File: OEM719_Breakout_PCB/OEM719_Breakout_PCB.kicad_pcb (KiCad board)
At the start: 2 copper layers, 165 x 61 mm, 27 parts, among them J1 Conn_02x10_Odd_Even, J2 Conn_02x10_Odd_Even, J3 Picoblade, J4 2.54mm Header, J5 2.54mm Socket

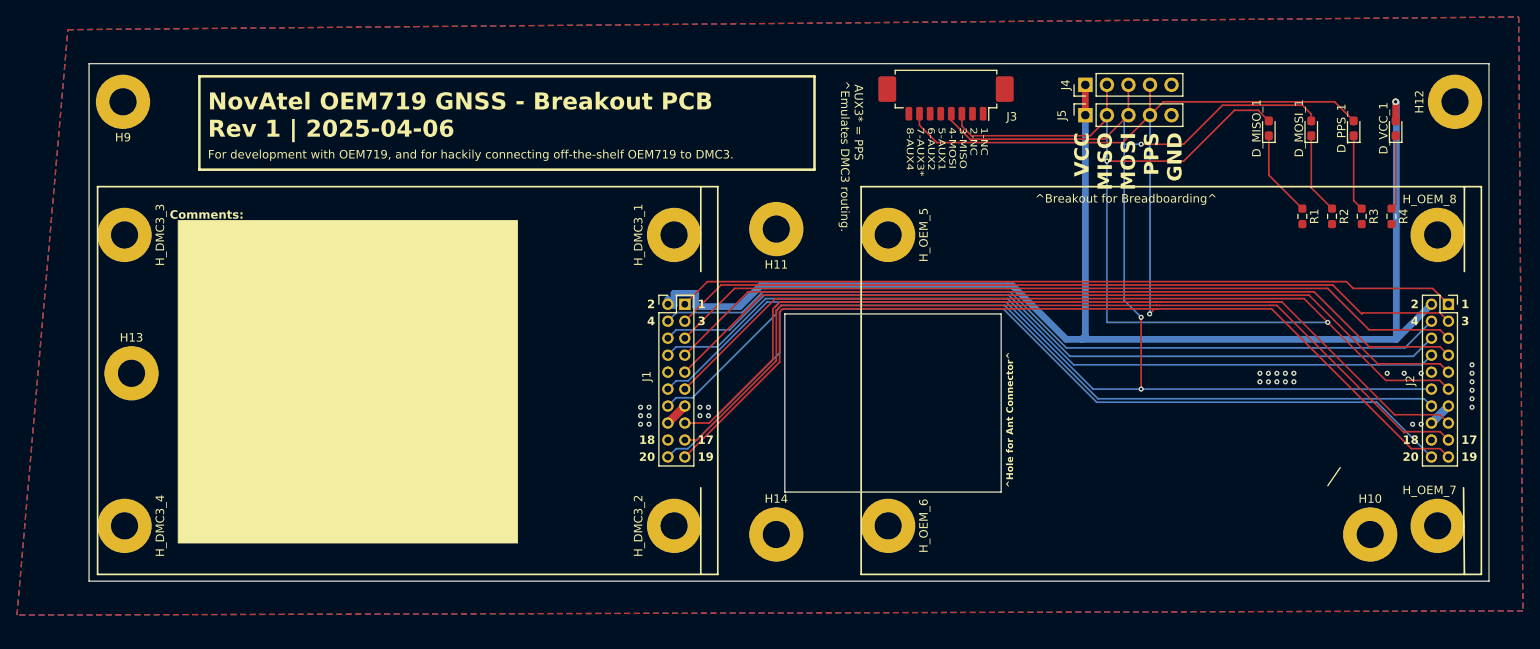
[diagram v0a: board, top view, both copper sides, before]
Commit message: Add 20-pin 2.54mm full breakout
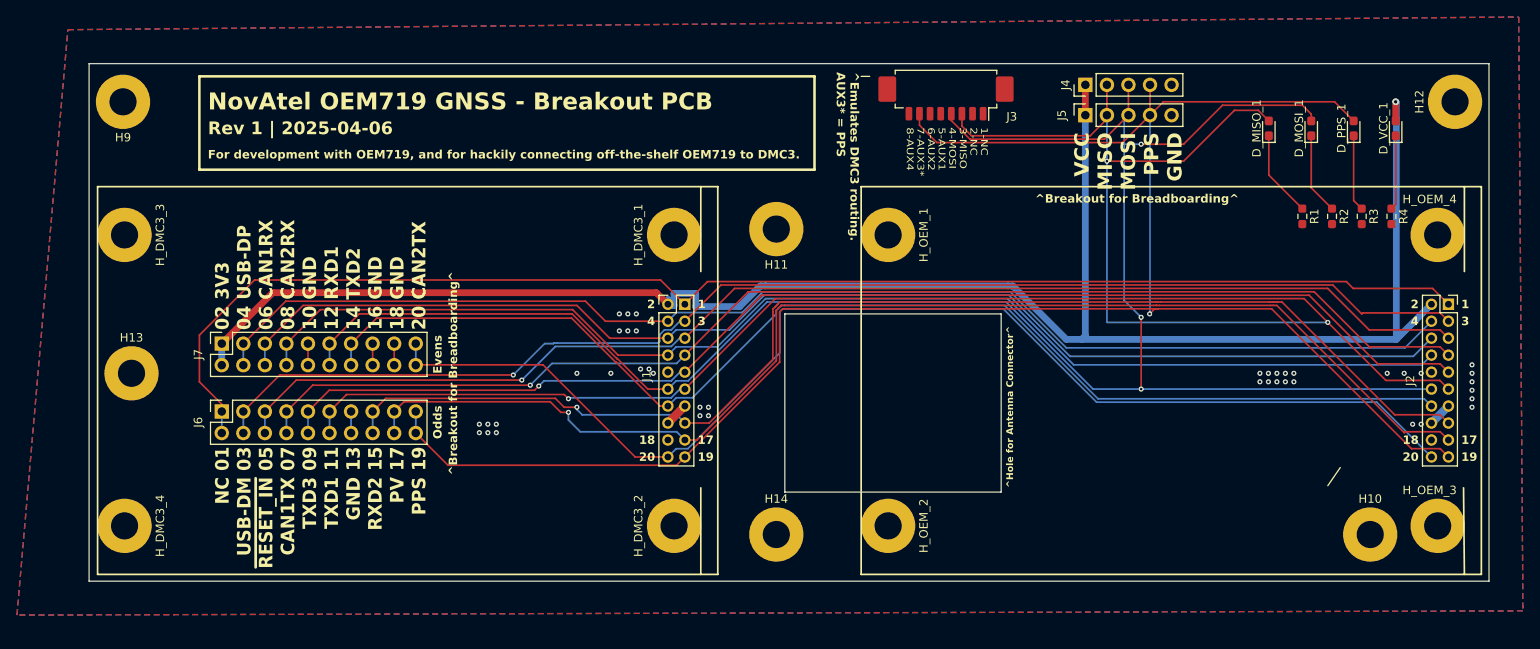
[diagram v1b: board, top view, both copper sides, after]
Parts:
- added J6: Conn_02x10_Odd_Even, 00-footprint-lib:PinHeaderSocket_2x10_P2.54mm_Vertical, F.Cu at (44.6, 111.5)
- added J7: Conn_02x10_Odd_Even, 00-footprint-lib:PinHeaderSocket_2x10_P2.54mm_Vertical, F.Cu at (44.6, 103.5)
- renumbered H_OEM_5 to H_OEM_1, H_OEM_6 to H_OEM_2, H_OEM_7 to H_OEM_3, H_OEM_8 to H_OEM_4
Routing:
- net PIN_1: track 92.2 -> 165.9 mm
- net PIN_3: track 93.6 -> 153.1 mm, vias 0 -> 1
- net PIN_2: track 159.6 -> 217.8 mm
- net PIN_4: track 95.5 -> 151.1 mm
- net PIN_5: track 94.9 -> 150.5 mm, vias 0 -> 1
- net PIN_6: track 96.0 -> 149.5 mm
- net PIN_7: track 96.3 -> 148.5 mm, vias 0 -> 1
- net PIN_8: track 96.5 -> 147.8 mm
- net PIN_9: track 97.6 -> 146.5 mm, vias 0 -> 1
- net PIN_12: track 184.4 -> 231.9 mm
- net PIN_11: track 195.2 -> 241.2 mm, vias 2 -> 3
- net PIN_14: track 100.1 -> 145.5 mm
- net PIN_15: track 105.3 -> 146.6 mm, vias 0 -> 1
- net PIN_17: track 106.7 -> 146.4 mm, vias 0 -> 1
- net PIN_20: track 107.6 -> 144.4 mm
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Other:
- board text added: "02 3V3 04 USB-DP 06 CAN1RX 08 CAN2RX 10 GND 12 RXD1 14 TXD2 16 GND 18 GND 20 CAN2TX"
- board text added: "20 CAN2TX 18 GND 16 GND 14 TXD2 12 RXD1 10 GND 08 CAN2RX 06 CAN1RX 04 USB-DP 02 3V3"
- board text added: "Evens"
- board text added: "NC 01 USB-DM 03 ~{RESET_IN} 05 CAN1TX 07 TXD3 09 TXD1 11 GND 13 RXD2 15 PV 17 PPS 19"
- board text added: "NovAtel OEM719 GNSS - Breakout PCB"
- board text added: "Odds"
- board text added: "PPS 19 PV 17 RXD2 15 GND 13 TXD1 11 TXD3 09 CAN1TX 07 ~{RESET_IN} 05 USB-DM 03 NC 01"
- board text added: "Rev 1 | 2025-04-06"
- board text added: "^Emulates DMC3 routing. AUX3* = PPS"
- board text added: "^Hole for Antenna Connector^"
- board text removed: "AUX3* = PPS ^Emulates DMC3 routing."
- board text removed: "Comments:"
- board text removed: "NovAtel OEM719 GNSS - Breakout PCB Rev 1 | 2025-04-06"
- board text removed: "^Hole for Ant Connector^"

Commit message: Add scale box for printout check
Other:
- board text added: "25.4mm x 6 inches"
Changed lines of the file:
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@@
 			(psa4output no)
 			(plot_black_and_white yes)
-			(plotinvisibletext no)
 			(sketchpadsonfab no)
 			(plotpadnumbers no)
@@
 	)
 	(gr_rect
+		(start 57.6 22.9)
+		(end 210 48.3)
+		(stroke
+			(width 0.01)
+			(type solid)
+		)
+		(fill yes)
+		(layer "Dwgs.User")
+	)
+	(gr_rect
 		(start 111 100)
 		(end 136.5 121)
@@
 		)
 	)
+	(gr_text "25.4mm x 6 inches"
+		(at 57.6 21.1 0)
+		(layer "Dwgs.User")
+		(effects
+			(font
+				(size 1 1)
+				(thickness 0.15)
+			)
+			(justify left bottom)
+		)
+	)
